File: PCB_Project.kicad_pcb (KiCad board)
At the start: 8 copper layers, 152.4 x 101.6 mm, 132 parts, among them J2 DF9-41P-1V32, J3 DF9-CFG-SPW1, J5 DF9-41P-1V32, J6 DF9-41P-1V32, U1 NX1H35 PBGA625, U2 CY15B108QN-40SXI, U3 M95P32-IXMNT/E, U4 CY15B108QN-40SXI, U5 AS4C8M32S-6TIN, U6 M95P32-IXMNT/E, U7 TPS3828-33DBVR, Y2 LFSPXO025225_25MHz

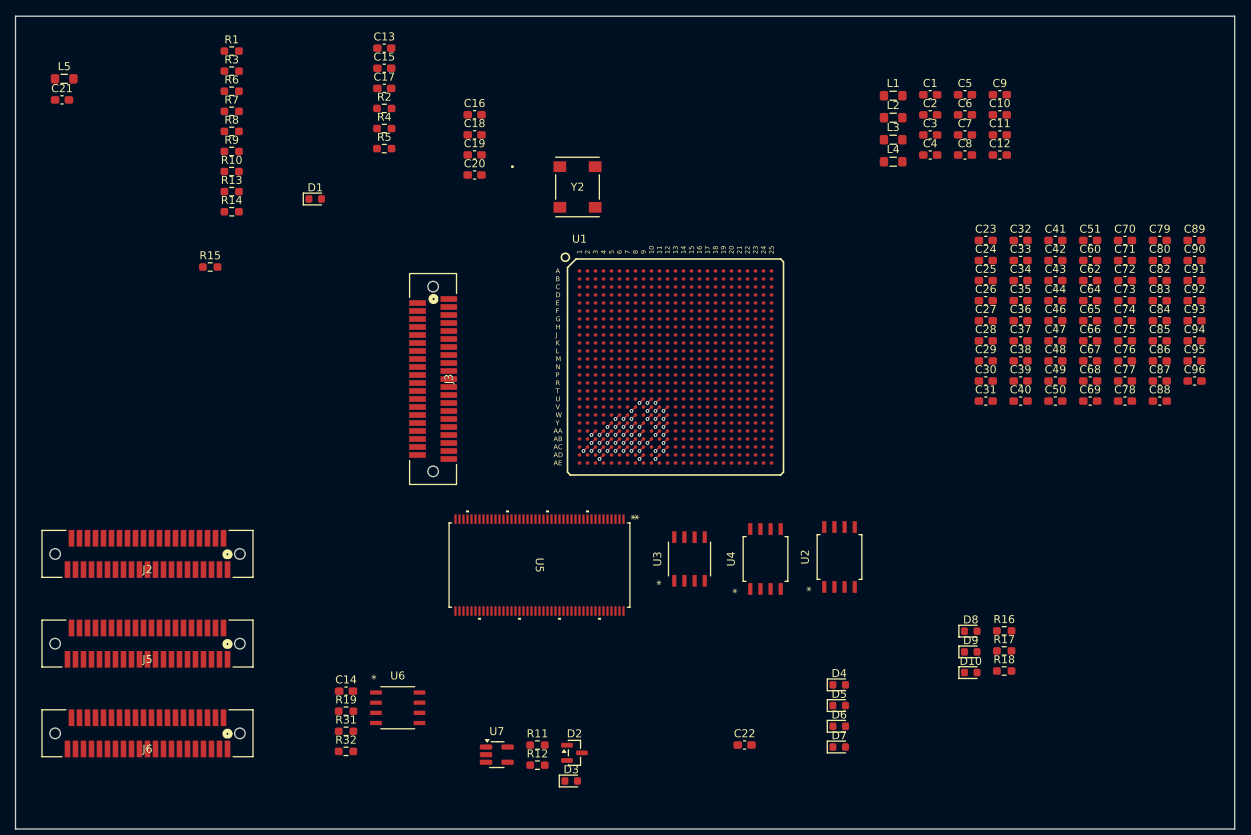
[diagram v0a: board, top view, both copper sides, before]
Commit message: first iteration of sdram
Fanout completed, started tracing towards the chip
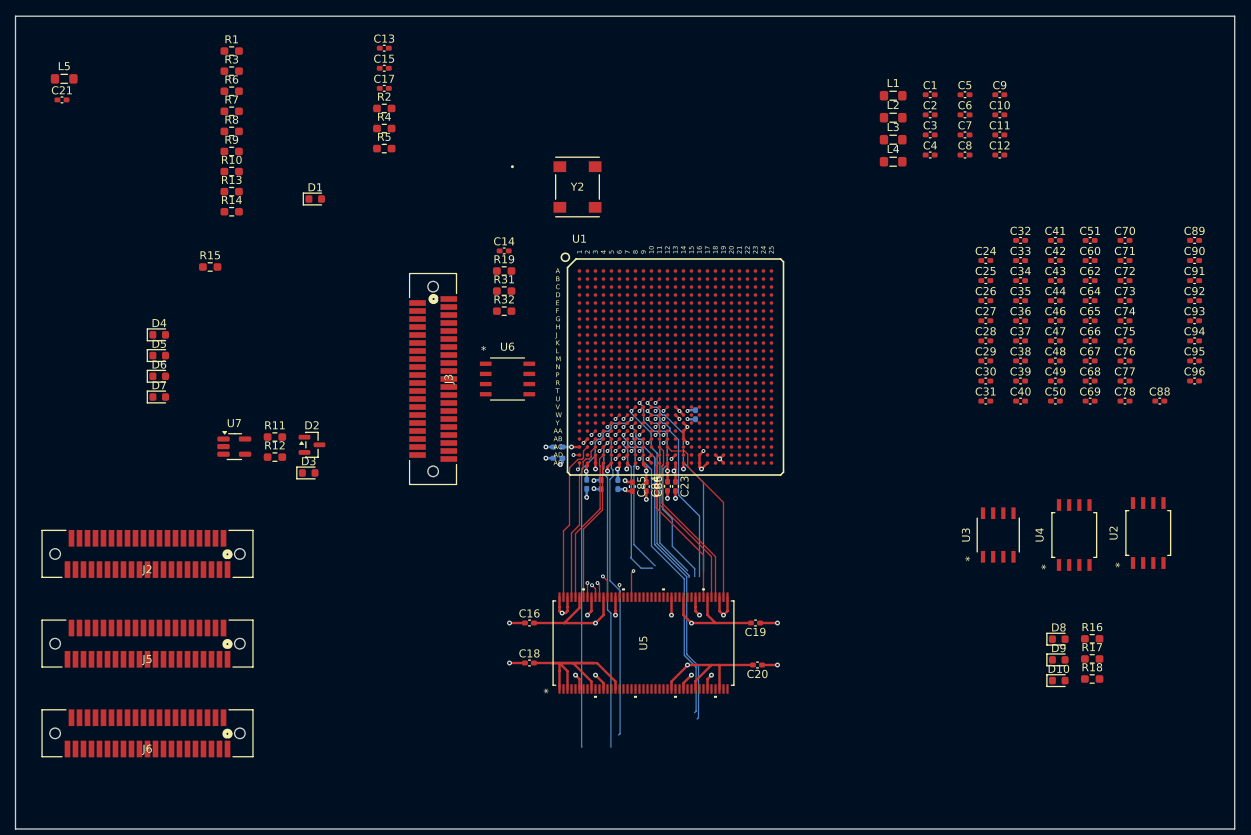
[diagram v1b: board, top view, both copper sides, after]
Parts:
- C1, C10, C11, C12, C13, C14, C15, C16, C17, C18, C19, C2, C20, C21, C23, C24, C25, C26, C27, C28, C29, C3, C30, C31, C32, C33, C34, C35, C36, C37, C38, C39, C4, C40, C41, C42, C43, C44, C46, C47, C48, C49, C5, C50, C51, C6, C60, C62, C64, C65, C66, C67, C68, C69, C7, C70, C71, C72, C73, C74, C75, C76, C77, C78, C8, C84, C85, C86, C88, C89, C9, C90, C91, C92, C93, C94, C95, C96: footprint Capacitor_SMD:C_0603_1608Metric_Pad1.08x0.95mm_HandSolder -> Capacitor_SMD:C_0402_1005Metric_Pad0.74x0.62mm_HandSolder
- C22, C79, C80, C82, C83, C87: footprint Capacitor_SMD:C_0603_1608Metric_Pad1.08x0.95mm_HandSolder -> Capacitor_SMD:C_0402_1005Metric_Pad0.74x0.62mm_HandSolder; moved to B.Cu
- moved D4 95.6 mm to (90.3, 94.0)
- moved D5 95.6 mm to (90.3, 96.6)
- moved D6 95.6 mm to (90.3, 99.2)
- moved D7 95.6 mm to (90.3, 101.8)
- moved C79 79.5 mm to (140.1, 108.1), turned to 180 degrees
- moved C83 77.8 mm to (140.1, 109.5), turned to 180 degrees
- moved C80 76.9 mm to (143.7, 112.7), turned to -90 degrees
- moved C82 74.3 mm to (145.5, 112.8), turned to -90 degrees
- moved C20 70.7 mm to (165.1, 135.3), turned to 180 degrees
- moved C85 68.4 mm to (149.4, 113.0), turned to -90 degrees
- moved C19 68.2 mm to (164.8, 130.1), turned to 180 degrees
- moved C84 67.5 mm to (151.2, 113.0), turned to -90 degrees
- moved C18 66.4 mm to (136.6, 135.1)
- moved C16 63.9 mm to (136.6, 130.1)
- moved C86 63.5 mm to (153.8, 113.0), turned to 90 degrees
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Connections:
- U1 pad A13: VDD2V5A -> VDD2V5
- U1 pad A20: VDD2V5A -> VDD2V5
- U1 pad A6: VDD2V5A -> VDD2V5
- U1 pad AE13: VDD2V5A -> VDD2V5
- U1 pad AE20: VDD2V5A -> VDD2V5
- U1 pad AE6: VDD2V5A -> VDD2V5
- U1 pad K1: VDD2V5A -> VDD2V5
- U1 pad K25: VDD2V5A -> VDD2V5
- U1 pad T1: VDD2V5A -> VDD2V5
- U1 pad T25: VDD2V5A -> VDD2V5
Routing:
- net /04_FPGA_Banks2_3_SDRAM/SDRAM_CAS_N: track 0.71 -> 90.4 mm
- net VDD3V3: track 0.00 -> 76.1 mm, vias 0 -> 3
- net GND: track 0.00 -> 61.3 mm, vias 0 -> 35
- net /04_FPGA_Banks2_3_SDRAM/SDRAM_CS_N: track 0.71 -> 45.7 mm
- net /04_FPGA_Banks2_3_SDRAM/SDRAM_A1: track 0.71 -> 42.8 mm
- net /04_FPGA_Banks2_3_SDRAM/SDRAM_A0: track 0.71 -> 42.7 mm
- net /04_FPGA_Banks2_3_SDRAM/SDRAM_DQ4: track 0.71 -> 42.7 mm
- net /04_FPGA_Banks2_3_SDRAM/SDRAM_RAS_N: track 0.71 -> 42.6 mm
- net /04_FPGA_Banks2_3_SDRAM/SDRAM_DQ5: track 0.71 -> 41.8 mm
- net /04_FPGA_Banks2_3_SDRAM/SDRAM_DQ16: track 0.71 -> 40.9 mm
- net /04_FPGA_Banks2_3_SDRAM/SDRAM_DQ3: track 0.71 -> 39.6 mm
- net /04_FPGA_Banks2_3_SDRAM/SDRAM_DQM2: track 0.71 -> 39.4 mm
- net /04_FPGA_Banks2_3_SDRAM/SDRAM_A2: track 0.71 -> 39.2 mm
- net /04_FPGA_Banks2_3_SDRAM/SDRAM_DQ17: track 0.71 -> 39.1 mm
- net /04_FPGA_Banks2_3_SDRAM/SDRAM_DQ0: track 0.71 -> 38.8 mm
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
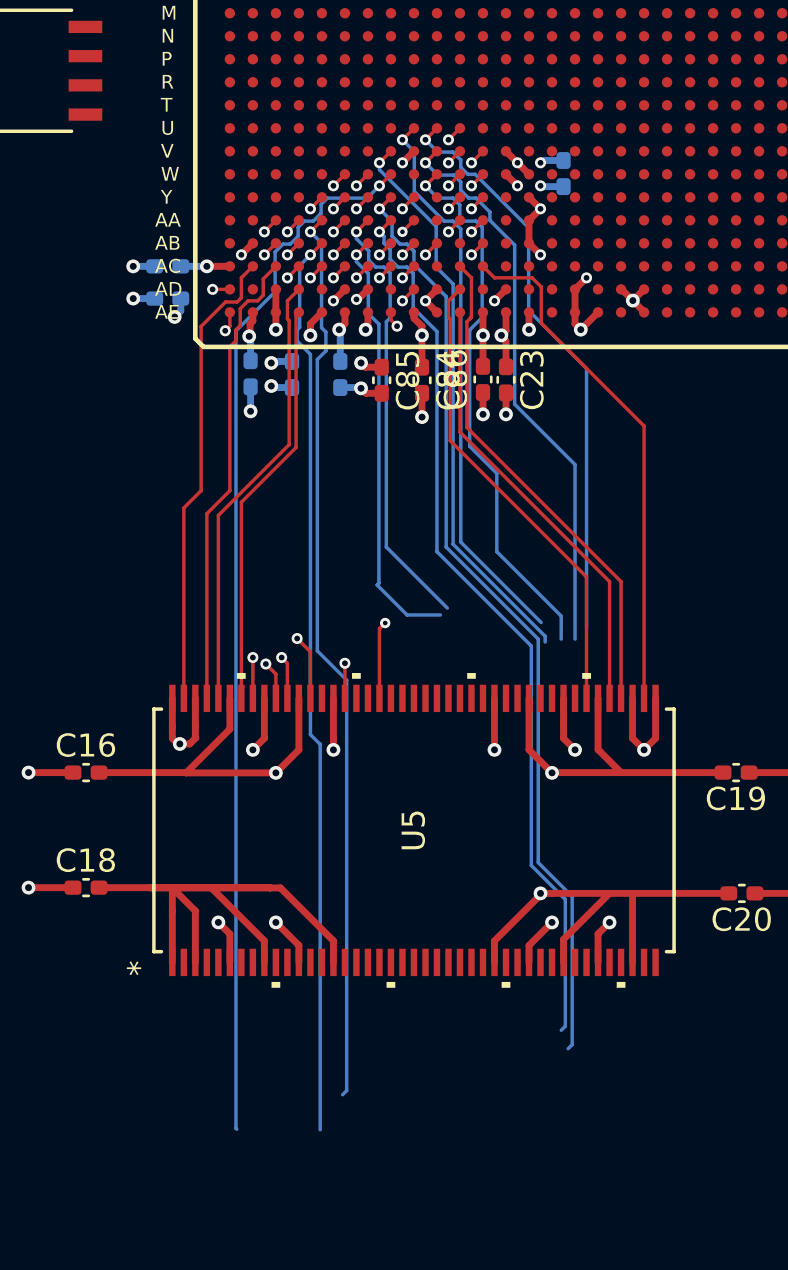
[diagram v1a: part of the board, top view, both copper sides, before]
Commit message: iteration 2 sdram
finished connections with sdram. shortened and adjusted as much as possible the traces.
straightened the traces.
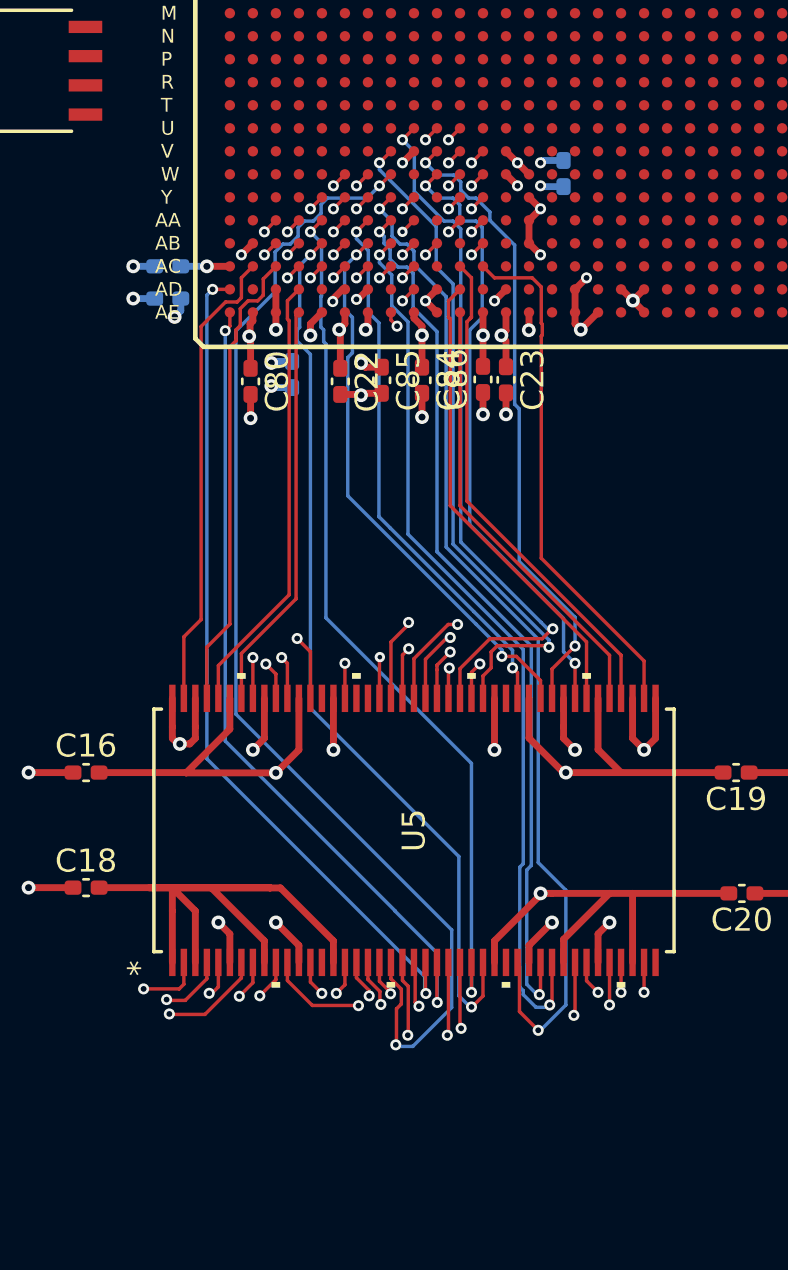
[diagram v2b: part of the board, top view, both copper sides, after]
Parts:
- C22, C80: moved to F.Cu
- moved C80 0.33 mm to (143.7, 113.1)
- moved C22 0.30 mm to (147.6, 113.1)
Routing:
- net /04_FPGA_Banks2_3_SDRAM/SDRAM_CAS_N: track 90.4 -> 41.4 mm, vias 1 -> 2
- net /04_FPGA_Banks2_3_SDRAM/SDRAM_DQ18: track 0.71 -> 38.9 mm, vias 1 -> 2
- net /04_FPGA_Banks2_3_SDRAM/SDRAM_DQ19: track 38.8 -> 46.0 mm, vias 1 -> 2
- net /04_FPGA_Banks2_3_SDRAM/SDRAM_A4: track 24.4 -> 31.1 mm, vias 1 -> 2
- net /04_FPGA_Banks2_3_SDRAM/SDRAM_CS_N: track 45.7 -> 51.3 mm, vias 1 -> 2
- net /04_FPGA_Banks2_3_SDRAM/SDRAM_DQ30: track 18.8 -> 24.3 mm, vias 1 -> 2
- net /04_FPGA_Banks2_3_SDRAM/SDRAM_DQM3: track 24.5 -> 29.6 mm, vias 1 -> 2
- net /04_FPGA_Banks2_3_SDRAM/SDRAM_A0: track 42.7 -> 47.8 mm, vias 1 -> 2
- net /04_FPGA_Banks2_3_SDRAM/SDRAM_DQ31: track 19.0 -> 23.9 mm, vias 1 -> 2
- net /04_FPGA_Banks2_3_SDRAM/SDRAM_RAS_N: track 42.6 -> 37.9 mm, vias 1 -> 2
- net /04_FPGA_Banks2_3_SDRAM/SDRAM_A10: track 31.0 -> 35.6 mm, vias 1 -> 2
- net /04_FPGA_Banks2_3_SDRAM/SDRAM_A11: track 37.0 -> 41.7 mm, vias 1 -> 2
- net /04_FPGA_Banks2_3_SDRAM/SDRAM_A7: track 22.2 -> 26.7 mm, vias 1 -> 2
- net /04_FPGA_Banks2_3_SDRAM/SDRAM_A6: track 22.9 -> 27.4 mm, vias 1 -> 2
- net /04_FPGA_Banks2_3_SDRAM/SDRAM_BA0: track 35.7 -> 40.1 mm, vias 1 -> 2
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
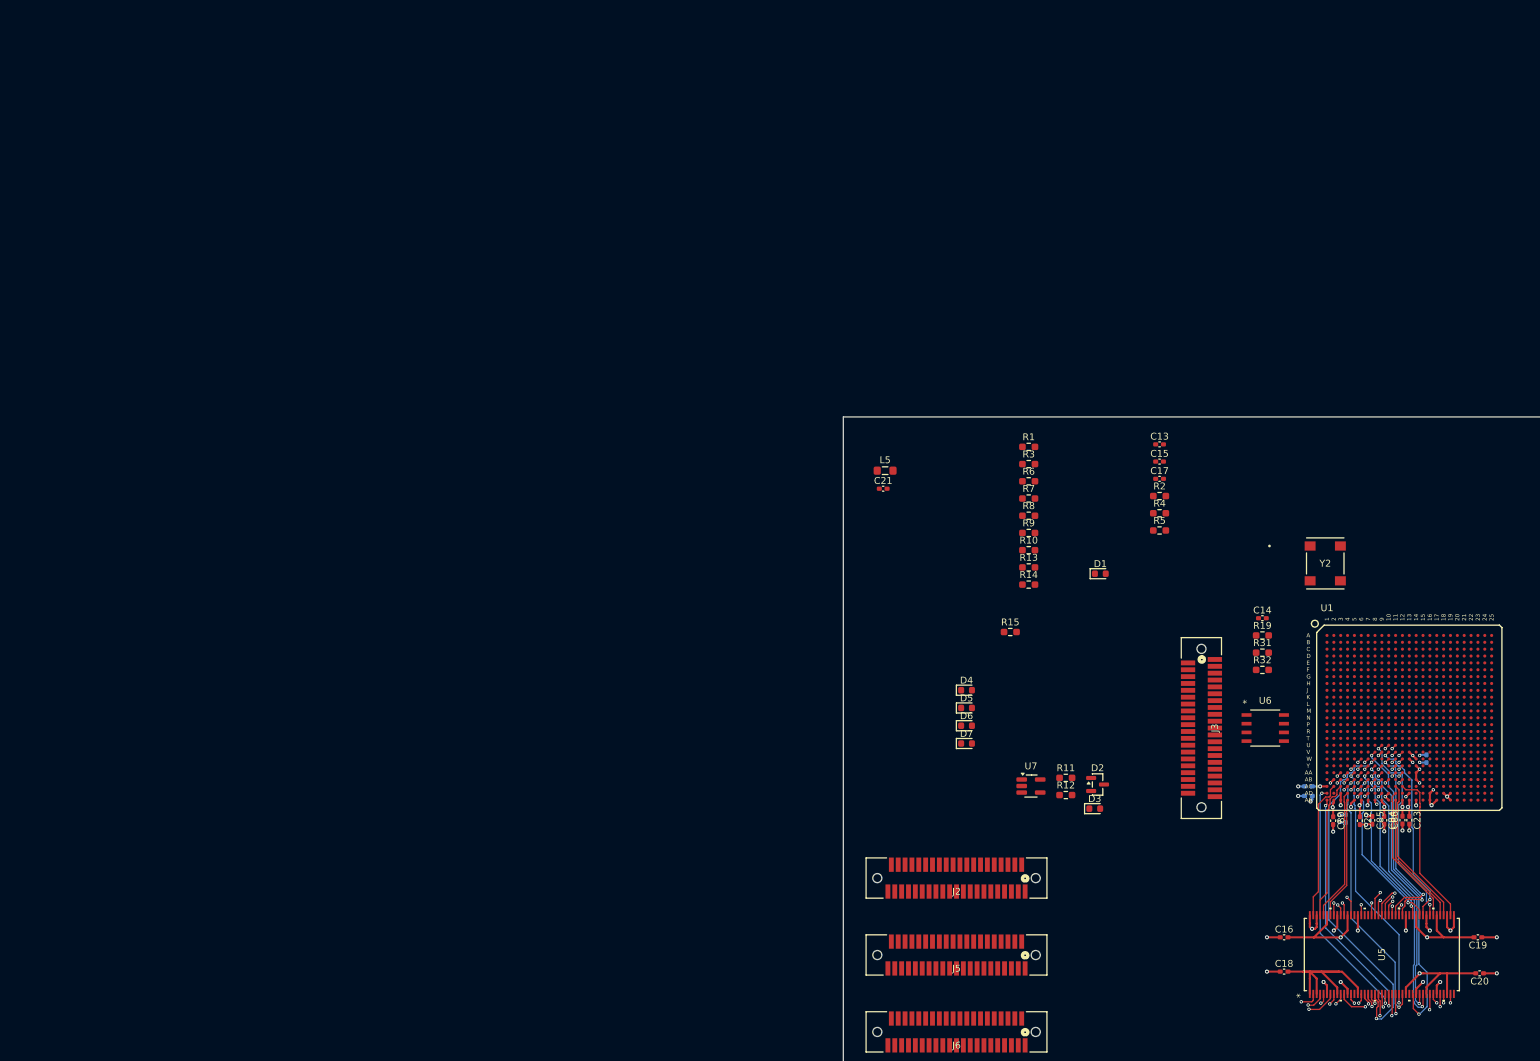
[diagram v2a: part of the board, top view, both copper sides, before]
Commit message: SDRAM iteration 3
finalized SDRAM connections and placement. optimized space and connectivity.
TBD:
iteration 4 will be regarding a reconfiguration of the pinout to try out a more optimal tracing.
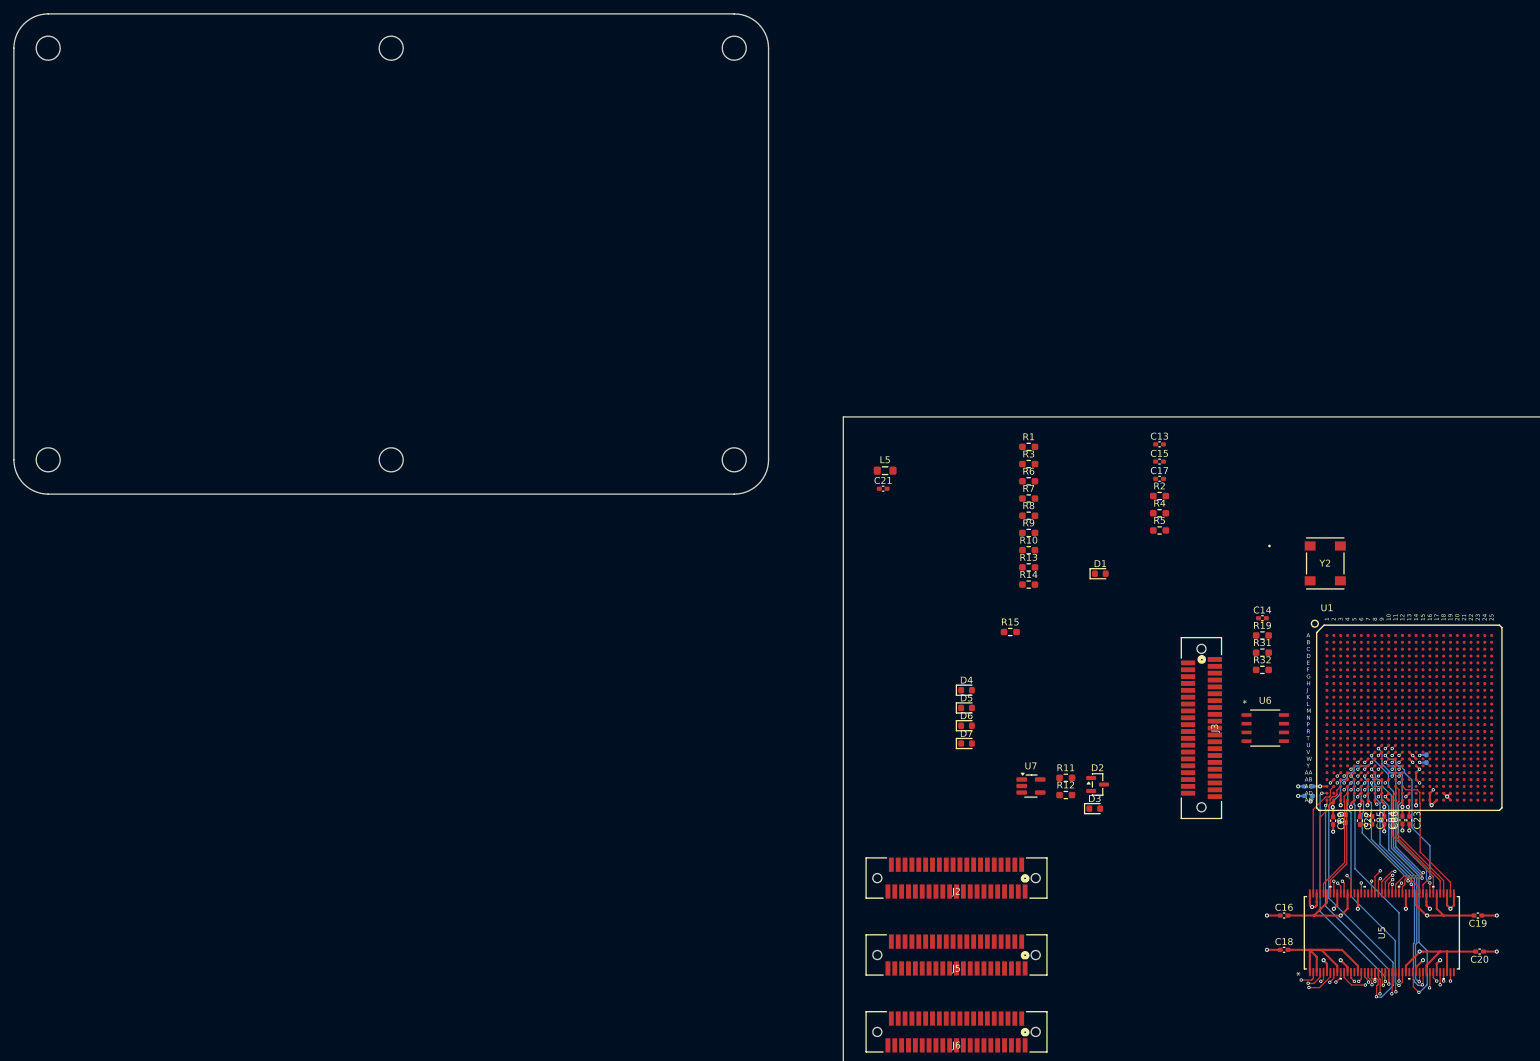
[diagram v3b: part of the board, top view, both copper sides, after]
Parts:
- added REF**: PCBoard, DataHub_Footprints:PCBoard, F.Cu at (6.40, 65.5)
- moved C16 3.17 mm to (136.6, 126.9)
- moved C18 3.17 mm to (136.6, 131.9)
- moved C19 3.17 mm to (164.8, 126.9)
- moved C20 3.17 mm to (165.1, 132.1)
- moved U5 3.17 mm to (150.8, 129.4)
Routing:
- net /04_FPGA_Banks2_3_SDRAM/SDRAM_DQM1: track 23.3 -> 19.8 mm
- net /04_FPGA_Banks2_3_SDRAM/SDRAM_A1: track 46.6 -> 43.3 mm
- net /04_FPGA_Banks2_3_SDRAM/SDRAM_BA0: track 40.1 -> 36.8 mm
- net /04_FPGA_Banks2_3_SDRAM/SDRAM_DQ24: track 22.8 -> 19.6 mm
- net /04_FPGA_Banks2_3_SDRAM/SDRAM_DQ22: track 38.8 -> 35.6 mm
- net /04_FPGA_Banks2_3_SDRAM/SDRAM_DQ21: track 39.4 -> 36.2 mm
- net /04_FPGA_Banks2_3_SDRAM/SDRAM_DQ6: track 38.8 -> 35.7 mm
- net /04_FPGA_Banks2_3_SDRAM/SDRAM_DQ17: track 38.6 -> 35.4 mm
- net /04_FPGA_Banks2_3_SDRAM/SDRAM_A10: track 35.6 -> 32.5 mm
- net /04_FPGA_Banks2_3_SDRAM/SDRAM_DQ7: track 34.6 -> 31.4 mm
- net /04_FPGA_Banks2_3_SDRAM/SDRAM_DQ28: track 26.8 -> 23.7 mm
- net /04_FPGA_Banks2_3_SDRAM/SDRAM_DQ27: track 20.5 -> 17.3 mm
- net /04_FPGA_Banks2_3_SDRAM/SDRAM_DQ14: track 20.3 -> 17.1 mm
- net /04_FPGA_Banks2_3_SDRAM/SDRAM_WE_N: track 32.0 -> 28.8 mm
- net /04_FPGA_Banks2_3_SDRAM/SDRAM_DQM2: track 39.0 -> 35.8 mm
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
